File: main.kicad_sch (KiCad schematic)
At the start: 29 parts, among them J1 Conn_01x02_Pin, U1 LMC555CMMX, U2 TPS7B8133QWDRVRQ1, U3 LT8374RUFM-WPBF

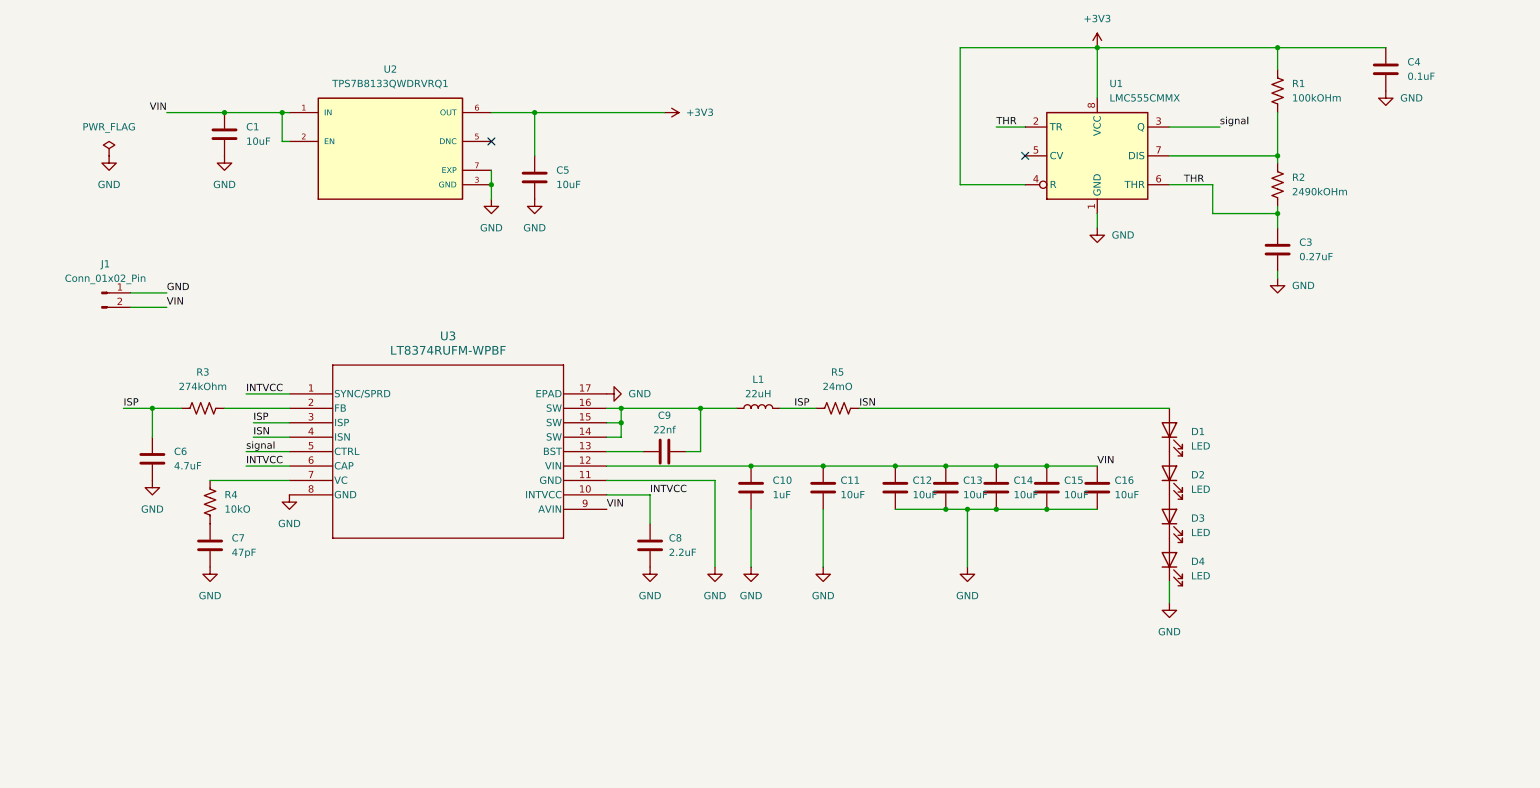
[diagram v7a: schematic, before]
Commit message: Adding in voltage divider for signal and layout and prod files
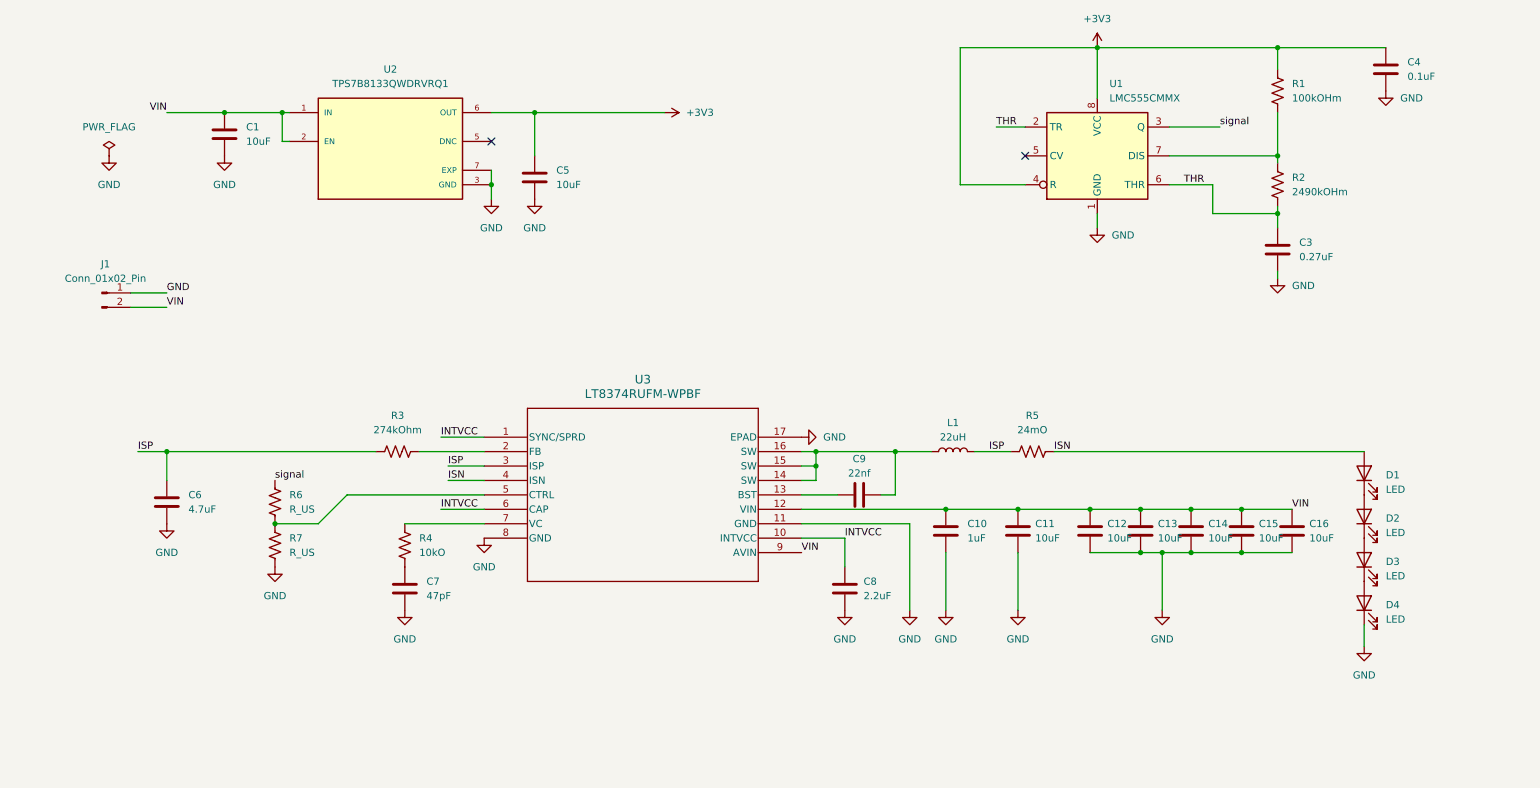
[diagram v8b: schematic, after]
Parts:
- added R6, R7: R_US, Resistor_SMD:R_0402_1005Metric, symbol Device:R_US
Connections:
- net GND: now also R7.2
- net signal: now also R6.1; no longer U3.5 (CTRL)
- new net: R6.2, R7.1, U3.5 (CTRL)
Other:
- moved on the sheet: C10, C11, C12, C13, C14, C15, C16, C6, C7, C8, C9, D1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
